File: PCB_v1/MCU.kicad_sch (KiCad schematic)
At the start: 53 parts, among them SW1 SW_Push, SW2 SW_Push, U1 STM32F407VGT6

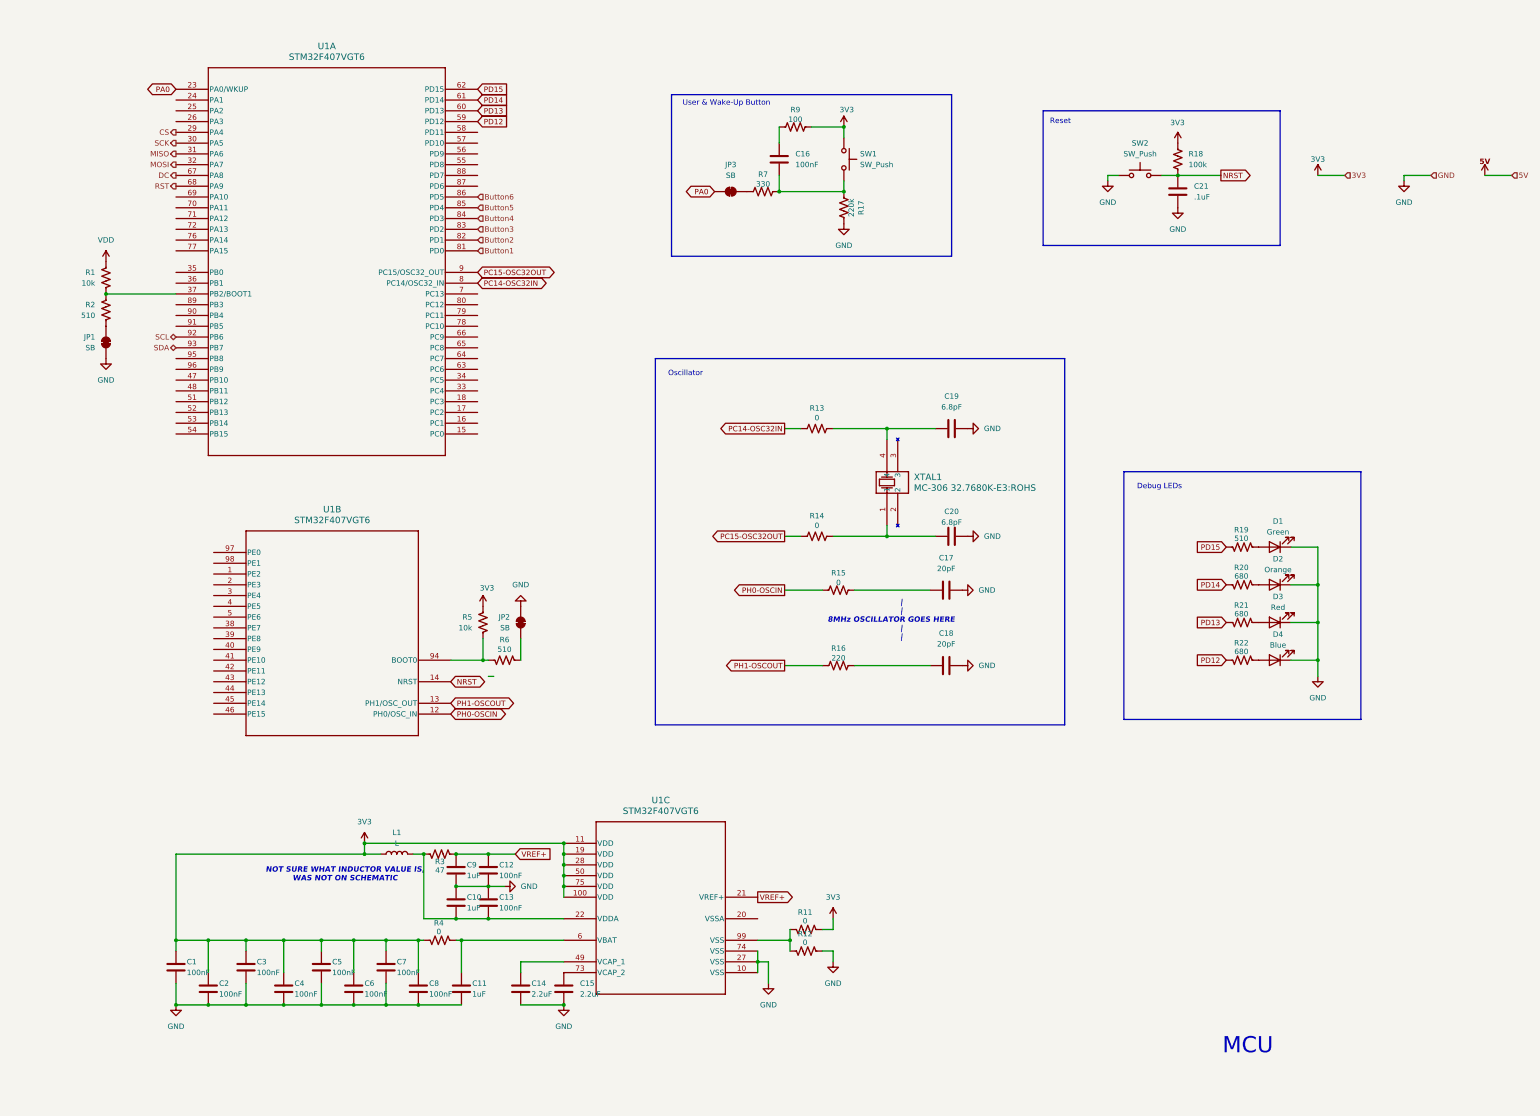
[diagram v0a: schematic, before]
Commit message: adding the parts library
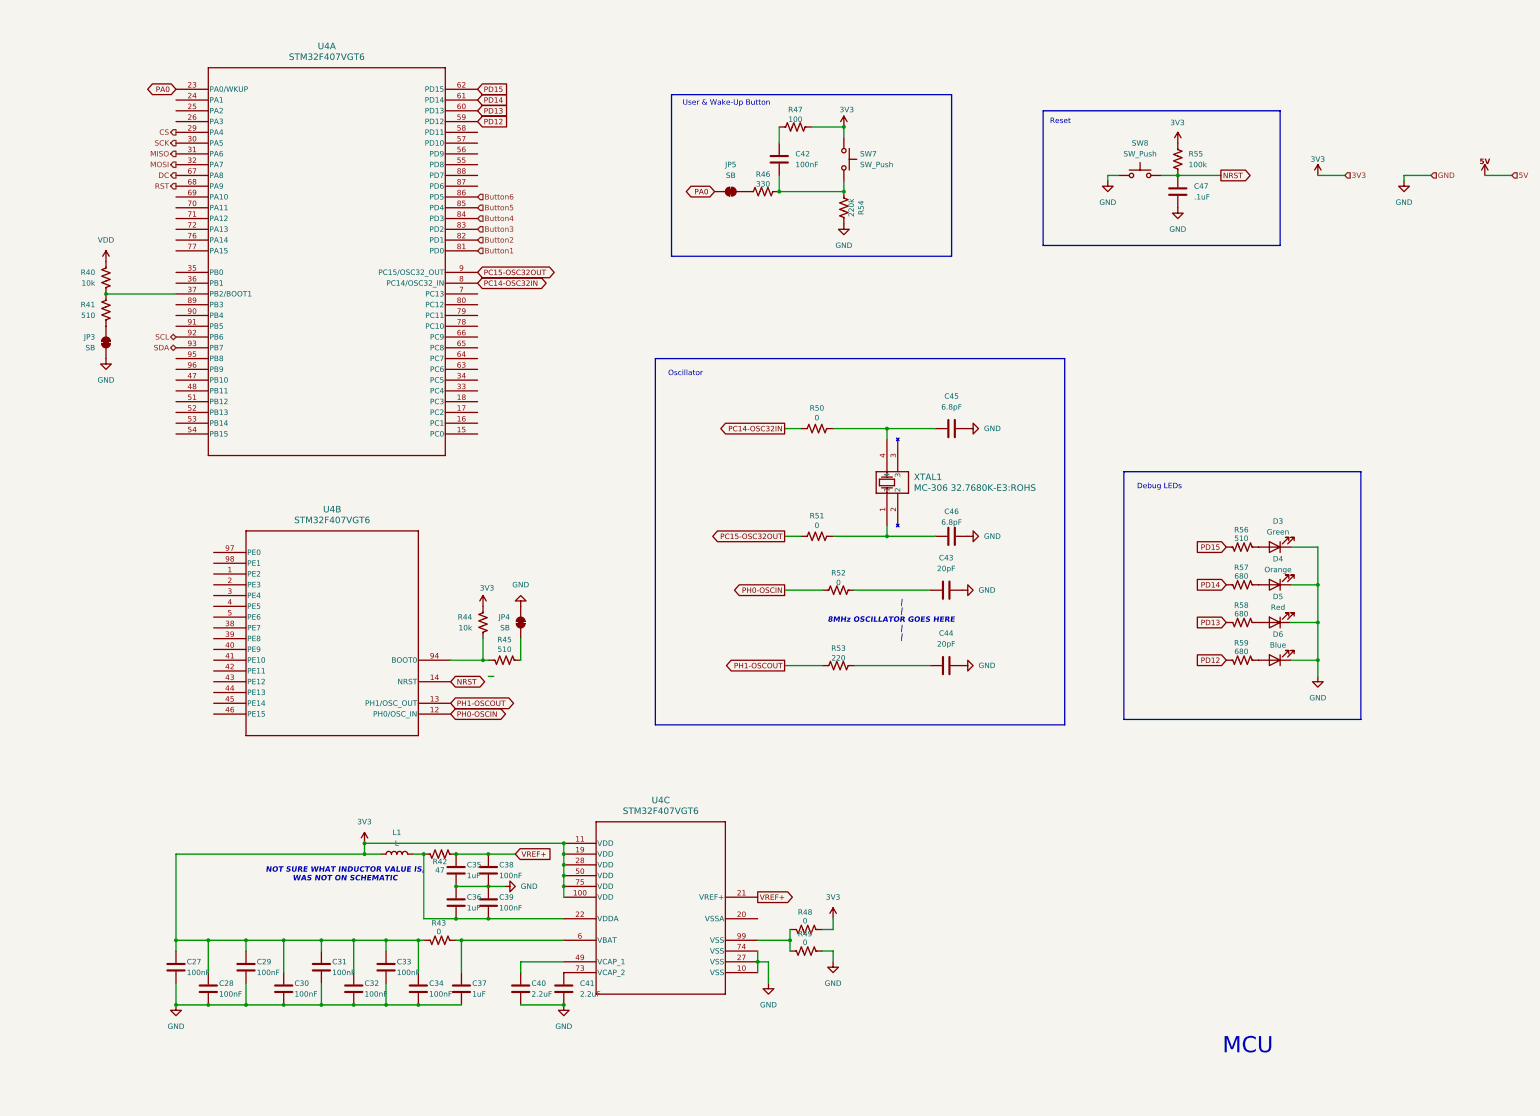
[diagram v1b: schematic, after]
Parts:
- U4: renamed from U1; footprint STM32F407VG6:LQFP100_14x14_STM -> LQFP100_14x14_STM
- renumbered C1 to C27, C2 to C28, C3 to C29, C4 to C30, C5 to C31, C6 to C32, C7 to C33, C8 to C34, C9 to C35, C10 to C36, C11 to C37, C12 to C38, C13 to C39, C14 to C40, C15 to C41, C16 to C42, C17 to C43, C18 to C44, C19 to C45, C20 to C46, C21 to C47, D1 to D3, D2 to D4, D3 to D5, D4 to D6, JP1 to JP3, JP2 to JP4, JP3 to JP5, R1 to R40, R2 to R41, R3 to R42, R4 to R43, R5 to R44, R6 to R45, R7 to R46, R9 to R47, R11 to R48, R12 to R49, R13 to R50, R14 to R51, R15 to R52, R16 to R53, R17 to R54, R18 to R55, R19 to R56, R20 to R57, R21 to R58, R22 to R59, SW1 to SW7, SW2 to SW8

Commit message: Updated UI w/ new header for OLED and updated MCU w/ STM32F405 and SWD (also some code I accdientally modified on this branch)
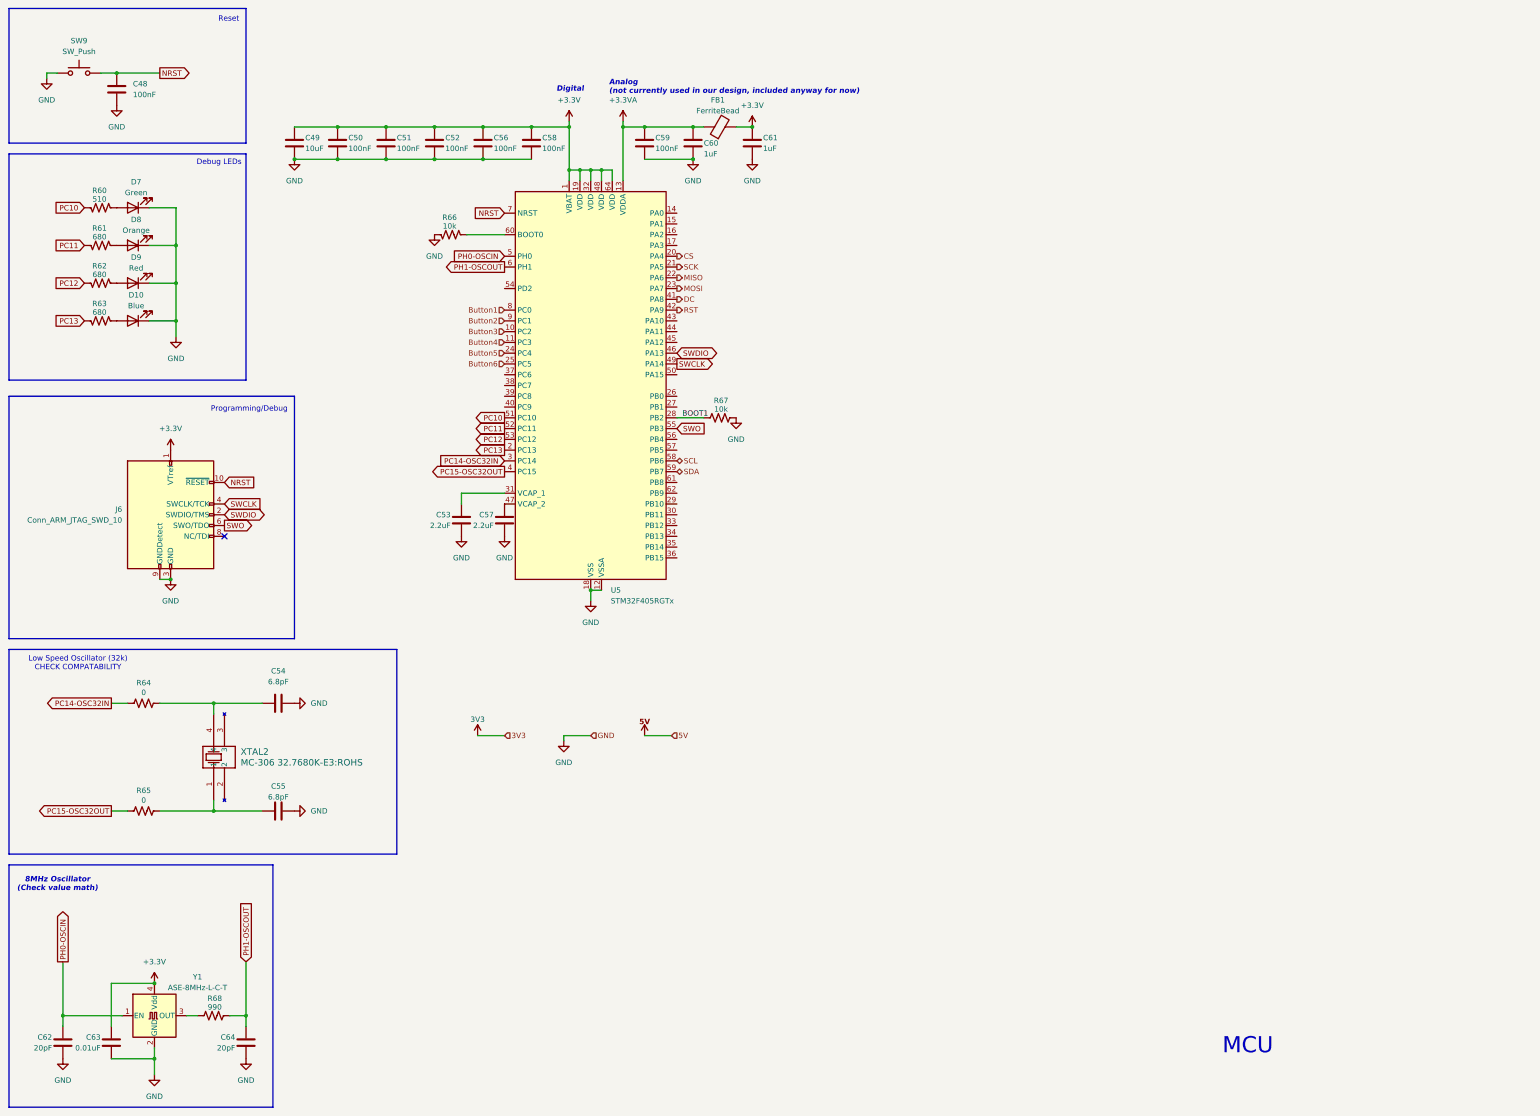
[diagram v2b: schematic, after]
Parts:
- removed C27, C28, C29, C30, C31, C32, C33, C34, C38, C39, C42: 100nF, Capacitor_SMD:C_0805_2012Metric, symbol Device:C
- removed C35, C36, C37: 1uF, Capacitor_SMD:C_0805_2012Metric, symbol Device:C
- removed C40, C41: 2.2uF, Capacitor_SMD:C_0805_2012Metric, symbol Device:C
- removed C43, C44: 20pF, Capacitor_SMD:C_0805_2012Metric, symbol Device:C
- removed C45, C46: 6.8pF, Capacitor_SMD:C_0805_2012Metric, symbol Device:C
- removed C47: .1uF, Capacitor_SMD:C_0805_2012Metric, symbol Device:C
- removed D3: Green, LED_SMD:LED_0805_2012Metric_Pad1.15x1.40mm_HandSolder, symbol Device:LED
- removed D4: Orange, LED_SMD:LED_0805_2012Metric_Pad1.15x1.40mm_HandSolder, symbol Device:LED
- removed D5: Red, LED_SMD:LED_0805_2012Metric_Pad1.15x1.40mm_HandSolder, symbol Device:LED
- removed D6: Blue, LED_SMD:LED_0805_2012Metric_Pad1.15x1.40mm_HandSolder, symbol Device:LED
- removed JP3, JP4, JP5: SB, Jumper:SolderJumper-2_P1.3mm_Bridged_Pad1.0x1.5mm, symbol Jumper:SolderJumper_2_Bridged
- removed L1: L, Inductor_SMD:L_0805_2012Metric, symbol Device:L
- removed R40, R44: 10k, Resistor_SMD:R_0805_2012Metric, symbol Device:R_US
- removed R41, R45, R56: 510, Resistor_SMD:R_0805_2012Metric, symbol Device:R_US
- removed R42: 47, Resistor_SMD:R_0805_2012Metric, symbol Device:R_US
- removed R43, R48, R49, R50, R51, R52: 0, Resistor_SMD:R_0805_2012Metric, symbol Device:R_US
- removed R46: 330, Resistor_SMD:R_0805_2012Metric, symbol Device:R_US
- removed R47: 100, Resistor_SMD:R_0805_2012Metric, symbol Device:R_US
- removed R53: 220, Resistor_SMD:R_0805_2012Metric, symbol Device:R_US
- removed R54: 220k, Resistor_SMD:R_0805_2012Metric, symbol Device:R_US
- removed R55: 100k, Resistor_SMD:R_0805_2012Metric, symbol Device:R_US
- removed R57, R58, R59: 680, Resistor_SMD:R_0805_2012Metric, symbol Device:R_US
- removed SW7, SW8: SW_Push, Button_Switch_SMD:SW_Push_1P1T_NO_CK_PTS125Sx43PSMTR, symbol Switch:SW_Push
- removed U4: STM32F407VGT6, LQFP100_14x14_STM, symbol STM32F407VG6:STM32F407VGT6
- removed XTAL1: MC-306 32.7680K-E3:ROHS, MC306:SO4_MC-306_SEC, symbol MC306:MC-306_32.7680K-E3_ROHS
- added C48, C50, C51, C52, C56, C58, C59: 100nF, Capacitor_SMD:C_0805_2012Metric, symbol Device:C
- added C49: 10uF, Capacitor_SMD:C_0805_2012Metric, symbol Device:C
- added C53, C57: 2.2uF, Capacitor_SMD:C_0805_2012Metric, symbol Device:C
- added C54, C55: 6.8pF, Capacitor_SMD:C_0805_2012Metric, symbol Device:C
- added C60, C61: 1uF, Capacitor_SMD:C_0805_2012Metric, symbol Device:C
- added C62, C64: 20pF, Capacitor_SMD:C_0805_2012Metric, symbol Device:C
- added C63: 0.01uF, Capacitor_SMD:C_0805_2012Metric, symbol Device:C
- added D10: Blue, LED_SMD:LED_0805_2012Metric_Pad1.15x1.40mm_HandSolder, symbol Device:LED
- added D7: Green, LED_SMD:LED_0805_2012Metric_Pad1.15x1.40mm_HandSolder, symbol Device:LED
- added D8: Orange, LED_SMD:LED_0805_2012Metric_Pad1.15x1.40mm_HandSolder, symbol Device:LED
- added D9: Red, LED_SMD:LED_0805_2012Metric_Pad1.15x1.40mm_HandSolder, symbol Device:LED
- added FB1: FerriteBead, Inductor_SMD:L_0805_2012Metric, symbol Device:FerriteBead
- added J6: Conn_ARM_JTAG_SWD_10, Connector_PinHeader_1.27mm:PinHeader_2x05_P1.27mm_Vertical, symbol Connector:Conn_ARM_JTAG_SWD_10
- added R60: 510, Resistor_SMD:R_0805_2012Metric, symbol Device:R_US
- added R61, R62, R63: 680, Resistor_SMD:R_0805_2012Metric, symbol Device:R_US
- added R64, R65: 0, Resistor_SMD:R_0805_2012Metric, symbol Device:R_US
- added R66, R67: 10k, Resistor_SMD:R_0805_2012Metric, symbol Device:R_US
- added R68: 990, Resistor_SMD:R_0805_2012Metric, symbol Device:R_US
- added SW9: SW_Push, Button_Switch_SMD:SW_Push_1P1T_NO_CK_PTS125Sx43PSMTR, symbol Switch:SW_Push
- added U5: STM32F405RGTx, Package_QFP:LQFP-64_10x10mm_P0.5mm, symbol MCU_ST_STM32F4:STM32F405RGTx
- added XTAL2: MC-306 32.7680K-E3:ROHS, MC_306_32_7680K_E3_ROHS:SO4_MC-306_SEC, symbol MC306:MC-306_32.7680K-E3_ROHS
- added Y1: ASE-8MHz-L-C-T, CHIP_ASE-24_ABR, symbol Oscillator:ASE-xxxMHz
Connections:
- net Button1: now also U5.8 (PC0)
- net Button2: now also U5.9 (PC1)
- net Button3: now also U5.10 (PC2)
- net Button4: now also U5.11 (PC3)
- net Button5: now also U5.24 (PC4)
- net Button6: now also U5.25 (PC5)
- net CS: now also U5.20 (PA4)
- net DC: now also U5.41 (PA8)
- net GND: now also C48.2, C49.2, C50.2, C51.2, C52.2, C53.2, C54.2, C55.2, C56.2, C57.2, C58.2, C59.2, C60.2, C61.2, C62.2, C63.2, C64.2, D10.1 (K), D7.1 (K), D8.1 (K), D9.1 (K), J6.3 (GND), J6.5 (GND), J6.9 (GNDDetect), R66.2, R67.2, SW9.1, U5.12 (VSSA), U5.18 (VSS), U5.63 (VSS), Y1.2 (GND)
- net MISO: now also U5.22 (PA6)
- net MOSI: now also U5.23 (PA7)
- net NRST: now also C48.1, J6.10 (~{RESET}), SW9.2, U5.7 (NRST)
- net PC14-OSC32IN: now also R64.1, U5.3 (PC14)
- net PC15-OSC32OUT: now also R65.1, U5.4 (PC15)
- net PH0-OSCIN: now also C62.1, U5.5 (PH0), Y1.1 (EN)
- net PH1-OSCOUT: now also C64.1, R68.2, U5.6 (PH1)
- net RST: now also U5.42 (PA9)
- net SCK: now also U5.21 (PA5)
- net SCL: now also U5.58 (PB6)
- net SDA: now also U5.59 (PB7)
- new net: D9.2 (A), R62.1
- new net: D8.2 (A), R61.1
- new net: D10.2 (A), R63.1
- new net: C55.1, R65.2, XTAL2.1
- new net: D7.2 (A), R60.1
- new net: R66.1, U5.60 (BOOT0)
- new net: C53.1, U5.31 (VCAP_1)
- new net: R68.1, Y1.3 (OUT)
- new net: C54.1, R64.2, XTAL2.4
- new net: C57.1, U5.47 (VCAP_2)
- new net +3.3V: C49.1, C50.1, C51.1, C52.1, C56.1, C58.1, C61.1, C63.1, FB1.2, J6.1 (VTref), U5.1 (VBAT), U5.19 (VDD), U5.32 (VDD), U5.48 (VDD), U5.64 (VDD), Y1.4 (Vdd)
- new net +3.3VA: C59.1, C60.1, FB1.1, U5.13 (VDDA)
- new net BOOT1: R67.1, U5.28 (PB2)
- new net PC10: R60.2, U5.51 (PC10)
- new net PC11: R61.2, U5.52 (PC11)
- new net PC12: R62.2, U5.53 (PC12)
- new net PC13: R63.2, U5.2 (PC13)
- new net SWCLK: J6.4 (SWCLK/TCK), U5.49 (PA14)
- new net SWDIO: J6.2 (SWDIO/TMS), U5.46 (PA13)
- new net SWO: J6.6 (SWO/TDO), U5.55 (PB3)
- no-connect marks 0 -> 1
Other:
- note added: "8MHz Oscillator (Check value math)"
- note added: "Analog (not currently used in our design, included anyway for now)"
- note added: "Digital"
- note added: "Low Speed Oscillator (32k) CHECK COMPATABILITY"
- note added: "Programming/Debug"
- note removed: "NOT SURE WHAT INDUCTOR VALUE IS, WAS NOT ON SCHEMATIC"
- note removed: "Oscillator"
- note removed: "User & Wake-Up Button"
- note removed: "| | 8MHz OSCILLATOR GOES HERE | |"

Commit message: PCB changes before changing Seth's clock
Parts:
- added R21, R22, R23, R24: 22, Resistor_SMD:R_0805_2012Metric, symbol Device:R_US
- Y1: footprint CHIP_ASE-24_ABR -> Oscillator:Oscillator_SMD_Abracon_ASE-4Pin_3.2x2.5mm
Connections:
- net Button4: now also U5.37 (PC6); no longer U5.11 (PC3)
- net NRST: now also R21.1; no longer J6.10 (~{RESET})
- net SWCLK: now also R22.1; no longer J6.4 (SWCLK/TCK)
- net SWDIO: now also R23.1; no longer J6.2 (SWDIO/TMS)
- net SWO: now also R24.1; no longer J6.6 (SWO/TDO)
- net I2S2_CLK: now reaches U5.29 (PB10)
- net I2S2_WS: now reaches U5.33 (PB12)
- new net: J6.10 (~{RESET}), R21.2
- new net: J6.2 (SWDIO/TMS), R23.2
- new net: J6.4 (SWCLK/TCK), R22.2
- new net: J6.6 (SWO/TDO), R24.2
- new net I2S2_SD: U5.11 (PC3)
